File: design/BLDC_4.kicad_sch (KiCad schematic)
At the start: 31 parts, among them J1 Conn_01x03, J2 Conn_01x02, J3 Conn_02x06_Odd_Even, K1 SERVO, P101 CANBUS, P3 PWR_COMM, X1 MINI-USB-SHIELD-32005-201

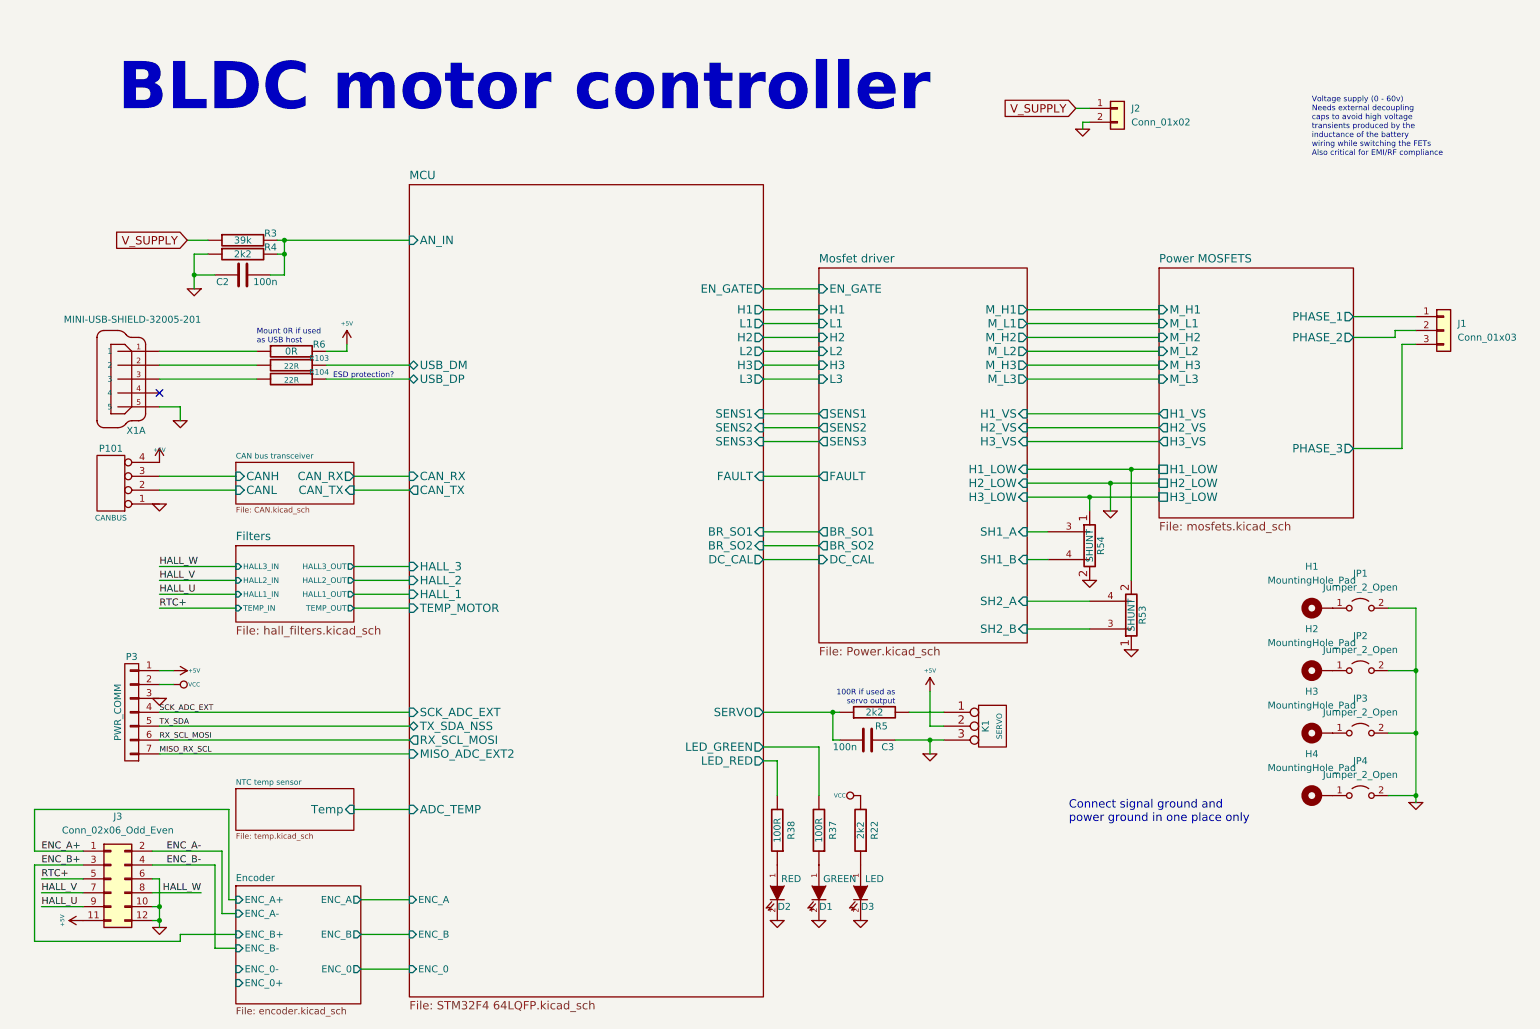
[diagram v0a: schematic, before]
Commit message: STM pins connected
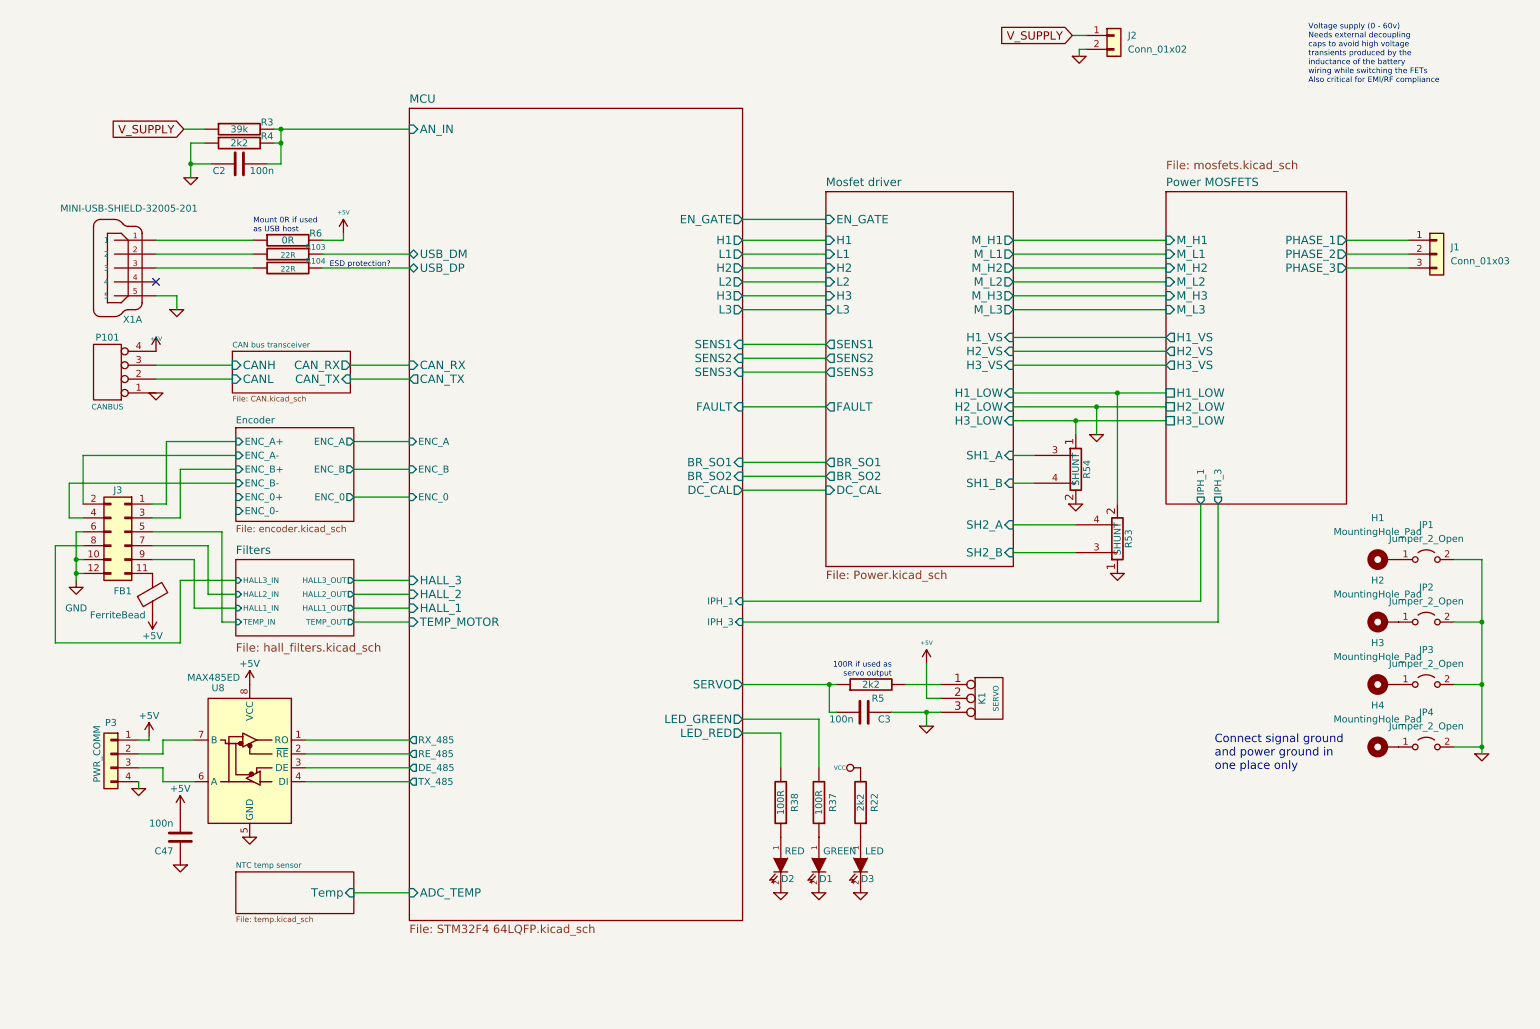
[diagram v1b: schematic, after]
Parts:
- added C47: 100n, CRF1:SMD-0603_c, symbol BLDC_4-rescue:C-RESCUE-BLDC_4
- added FB1: FerriteBead, Resistor_SMD:R_0805_2012Metric, symbol Device:FerriteBead
- added U8: MAX485ED, Package_SO:SOIC-8_3.9x4.9mm_P1.27mm, symbol Interface_UART:MAX485E
- P3: footprint CRF1:b7b-ph-kl -> Connector_JST:JST_PH_S4B-PH-K_1x04_P2.00mm_Horizontal; symbol BLDC_4-rescue:CONN_01X07 -> Connector_Generic:Conn_01x04
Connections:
- net SCK_ADC_EXT is gone; now on net GND: P3.4 (Pin_4)
- net +5V: now also C47.2, FB1.1, U8.8 (VCC); no longer J3.11 (Pin_11)
- net GND: now also C47.1, U8.5 (GND); no longer P3.3 (P3)
- net VCC: no longer P3.2 (P2)
- net ENC_A+ renamed Encoder/ENC_A+
- net ENC_A- renamed Encoder/ENC_A-
- net ENC_B+ renamed Encoder/ENC_B+
- net ENC_B- renamed Encoder/ENC_B-
- net HALL_U renamed Filters/HALL1_IN
- net HALL_V renamed Filters/HALL2_IN
- net HALL_W renamed Filters/HALL3_IN
- removed net MISO_RX_SCL: P3.7 (P7)
- net RTC+ renamed Filters/TEMP_IN
- removed net RX_SCL_MOSI: P3.6 (P6)
- removed net TX_SDA: P3.5 (P5)
- new net: P3.2 (Pin_2), U8.7 (B)
- new net: P3.3 (Pin_3), U8.6 (A)
- new net: FB1.2, J3.11 (Pin_11)
- new net MCU/DE_485: U8.3 (DE)
- new net MCU/RE_485: U8.2 (~{RE})
- new net MCU/RX_485: U8.1 (RO)
- new net MCU/TX_485: U8.4 (DI)
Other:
- sheet MCU ports: added DE_485, IPH_1, IPH_3, RE_485, RX_485, TX_485; removed MISO_ADC_EXT2, RX_SCL_MOSI, SCK_ADC_EXT, TX_SDA_NSS
- sheet Power MOSFETS ports: added IPH_1, IPH_3; removed none
- note removed: "BLDC motor controller"
- moved on the sheet: C2, C3, D1, D2, D3, H1, H2, H3, H4, J1, J2, JP1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

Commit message: Última versão de hoje
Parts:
- added J6: Conn_02x06_Odd_Even, Connector_JST:JST_PH_S2B-PH-K_1x02_P2.00mm_Horizontal, symbol Connector_Generic:Conn_01x02
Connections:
- net Encoder/ENC_0+: now also J6.1 (Pin_1)
- net Encoder/ENC_0-: now also J6.2 (Pin_2)
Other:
- moved on the sheet: J2
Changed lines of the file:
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@@
+    (stroke (width 0) (type default))
+  )
+  (wire (pts (xy 41.91 95.25) (xy 26.67 95.25))
     (stroke (width 0) (type default))
   )
@@
     (stroke (width 0) (type default))
   )
-  (wire (pts (xy 22.86 93.98) (xy 22.86 102.87))
-    (stroke (width 0) (type default))
-  )
   (wire (pts (xy 273.685 135.89) (xy 278.765 135.89))
     (stroke (width 0) (type default))
@@
     (stroke (width 0) (type default))
   )
+  (wire (pts (xy 50.8 101.6) (xy 44.45 101.6))
+    (stroke (width 0) (type default))
+  )
   (wire (pts (xy 53.975 54.61) (xy 36.195 54.61))
     (stroke (width 0) (type default))
@@
     (stroke (width 0) (type default))
   )
-  (wire (pts (xy 50.8 93.98) (xy 22.86 93.98))
-    (stroke (width 0) (type default))
-  )
   (wire (pts (xy 273.685 113.03) (xy 278.765 113.03))
     (stroke (width 0) (type default))
@@
     (stroke (width 0) (type default))
   )
-  (wire (pts (xy 206.375 19.685) (xy 205.105 19.685))
+  (wire (pts (xy 196.85 25.4) (xy 195.58 25.4))
     (stroke (width 0) (type default))
   )
@@
     (stroke (width 0) (type default))
   )
+  (wire (pts (xy 22.86 97.79) (xy 22.86 102.87))
+    (stroke (width 0) (type default))
+  )
   (wire (pts (xy 66.675 59.69) (xy 82.55 59.69))
     (stroke (width 0) (type default))
@@
     (stroke (width 0) (type default))
   )
+  (wire (pts (xy 44.45 92.71) (xy 26.67 92.71))
+    (stroke (width 0) (type default))
+  )
   (wire (pts (xy 158.75 59.69) (xy 143.51 59.69))
     (stroke (width 0) (type default))
@@
     (stroke (width 0) (type default))
   )
-  (wire (pts (xy 203.835 17.145) (xy 206.375 17.145))
+  (wire (pts (xy 194.31 22.86) (xy 196.85 22.86))
     (stroke (width 0) (type default))
   )
@@
     (stroke (width 0) (type default))
   )
-  (wire (pts (xy 205.105 19.685) (xy 205.105 20.955))
+  (wire (pts (xy 195.58 25.4) (xy 195.58 26.67))
     (stroke (width 0) (type default))
   )
@@
     (stroke (width 0) (type default))
   )
+  (wire (pts (xy 50.8 104.14) (xy 41.91 104.14))
+    (stroke (width 0) (type default))
+  )
   (wire (pts (xy 36.195 80.01) (xy 50.165 80.01))
     (stroke (width 0) (type default))
@@
     (stroke (width 0) (type default))
   )
+  (wire (pts (xy 33.02 97.79) (xy 33.02 93.98))
+    (stroke (width 0) (type default))
+  )
   (wire (pts (xy 37.465 151.13) (xy 37.465 153.67))
     (stroke (width 0) (type default))
@@
     (stroke (width 0) (type default))
   )
+  (wire (pts (xy 44.45 101.6) (xy 44.45 92.71))
+    (stroke (width 0) (type default))
+  )
   (wire (pts (xy 273.685 147.32) (xy 278.765 147.32))
     (stroke (width 0) (type default))
@@
     (stroke (width 0) (type default))
   )
+  (wire (pts (xy 33.02 97.79) (xy 22.86 97.79))
+    (stroke (width 0) (type default))
+  )
   (wire (pts (xy 40.005 64.77) (xy 36.195 64.77))
     (stroke (width 0) (type default))
@@
     (stroke (width 0) (type default))
   )
+  (wire (pts (xy 33.02 93.98) (xy 50.8 93.98))
+    (stroke (width 0) (type default))
+  )
   (wire (pts (xy 21.59 113.03) (xy 21.59 115.57))
+    (stroke (width 0) (type default))
+  )
+  (wire (pts (xy 41.91 104.14) (xy 41.91 95.25))
     (stroke (width 0) (type default))
   )
@@
     )
   )
-  (global_label "V_SUPPLY" (shape input) (at 203.835 17.145 180) (fields_autoplaced)
+  (global_label "V_SUPPLY" (shape input) (at 194.31 22.86 180) (fields_autoplaced)
     (effects (font (size 1.524 1.524)) (justify right))
-    (property "Intersheetrefs" "${INTERSHEET_REFS}" (at 434.975 -13.335 0)
+    (property "Intersheetrefs" "${INTERSHEET_REFS}" (at 425.45 -7.62 0)
       (effects (font (size 1.27 1.27)) (justify left) hide)
     )
@@
     )
   )
+  (symbol (lib_id "Connector_Generic:Conn_01x02") (at 21.59 92.71 0) (mirror y) (unit 1)
+    (in_bom yes) (on_board yes) (dnp no)
+    (property "Reference" "J6" (at 21.59 90.17 0)
+      (effects (font (size 1.27 1.27)))
+    )
+    (property "Value" "Conn_02x06_Odd_Even" (at -57.15 73.66 0)
+      (effects (font (size 1.27 1.27)) hide)
+    )
+    (property "Footprint" "Connector_JST:JST_PH_S2B-PH-K_1x02_P2.00mm_Horizontal" (at 21.59 92.71 0)
+      (effects (font (size 1.27 1.27)) hide)
+    )
+    (property "Datasheet" "~" (at 21.59 92.71 0)
+      (effects (font (size 1.27 1.27)) hide)
+    )
+    (pin "1")
+    (pin "2")
+    (instances
+      (project "BLDC_4"
+        (path "/f0823096-6b01-491e-b593-a00aa44575f0"
+          (reference "J6") (unit 1)
+        )
+      )
+    )
+  )
   (symbol (lib_id "Jumper:Jumper_2_Open") (at 268.605 147.32 0) (unit 1)
     (in_bom yes) (on_board yes) (dnp no) (fields_autoplaced)
@@
     )
   )
-  (symbol (lib_id "Connector_Generic:Conn_01x02") (at 211.455 17.145 0) (unit 1)
-    (in_bom yes) (on_board yes) (dnp no) (fields_autoplaced)
-    (property "Reference" "J2" (at 213.995 17.1449 0)
+  (symbol (lib_id "Connector_Generic:Conn_01x02") (at 201.93 22.86 0) (unit 1)
+    (in_bom yes) (on_board yes) (dnp no)
+    (property "Reference" "J2" (at 204.47 22.8599 0)
       (effects (font (size 1.27 1.27)) (justify left))
     )
-    (property "Value" "Conn_01x02" (at 213.995 19.6849 0)
+    (property "Value" "Conn_01x02" (at 204.47 25.3999 0)
       (effects (font (size 1.27 1.27)) (justify left))
     )
-    (property "Footprint" "Connector_Phoenix_MSTB:PhoenixContact_MSTBA_2,5_2-G-5,08_1x02_P5.08mm_Horizontal" (at 211.455 17.145 0)
-      (effects (font (size 1.27 1.27)) hide)
-    )
-    (property "Datasheet" "~" (at 211.455 17.145 0)
+    (property "Footprint" "Connector_Phoenix_MSTB:PhoenixContact_MSTBA_2,5_2-G-5,08_1x02_P5.08mm_Horizontal" (at 201.93 22.86 0)
+      (effects (font (size 1.27 1.27)) hide)
+    )
+    (property "Datasheet" "~" (at 201.93 22.86 0)
       (effects (font (size 1.27 1.27)) hide)
     )
@@
     )
   )
-  (symbol (lib_id "BLDC_4-rescue:GND-RESCUE-BLDC_4") (at 205.105 20.955 0) (unit 1)
-    (in_bom yes) (on_board yes) (dnp no)
-    (property "Reference" "#PWR018" (at 205.105 20.955 0)
-      (effects (font (size 0.762 0.762)) hide)
-    )
-    (property "Value" "GND" (at 205.105 22.733 0)
-      (effects (font (size 0.762 0.762)) hide)
-    )
-    (property "Footprint" "" (at 205.105 20.955 0)
-      (effects (font (size 1.524 1.524)) hide)
-    )
-    (property "Datasheet" "" (at 205.105 20.955 0)
-      (effects (font (size 1.524 1.524)) hide)
-    )
+  (symbol (lib_id "BLDC_4-rescue:GND-RESCUE-BLDC_4") (at 195.58 26.67 0) (unit 1)
+    (in_bom yes) (on_board yes) (dnp no)
+    (property "Reference" "#PWR018" (at 195.58 26.67 0)
+      (effects (font (size 0.762 0.762)) hide)
+    )
+    (property "Value" "GND" (at 195.58 28.448 0)
+      (effects (font (size 0.762 0.762)) hide)
+    )
+    (property "Footprint" "" (at 195.58 26.67 0)
+      (effects (font (size 1.524 1.524)) hide)
+    )
+    (property "Datasheet" "" (at 195.58 26.67 0)
+      (effects (font (size 1.524 1.524)) hide)
+    )

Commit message: Final 20230228
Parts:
- removed R53, R54: SHUNT, CRF1:WSLP2726, symbol BLDC_4-rescue:SHUNT
- added JP5, JP6, JP7, JP8: SolderJumper_2_Bridged, JRM_Footprint:MicroNetSep, symbol Jumper:SolderJumper_2_Bridged
- added R52, R53: YLR12-3-8F-W, JRM_Footprint:YLR2512_G4, symbol Device:R_US
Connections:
- net GND: now also JP5.2 (B), JP8.2 (B), R52.2, R53.2
- net Mosfet driver/H1_LOW: now also JP6.2 (B), R52.1
- net Mosfet driver/H3_LOW: now also JP7.2 (B), R53.1
- net Mosfet driver/SH1_A: now also JP7.1 (A)
- net Mosfet driver/SH1_B: now also JP8.1 (A)
- net Mosfet driver/SH2_A: now also JP6.1 (A)
- net Mosfet driver/SH2_B: now also JP5.1 (A)
